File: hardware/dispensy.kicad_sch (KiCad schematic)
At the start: 20 parts, among them SW3 UP, SW4 MENU, SW5 DOWN, U1 DBT50G-7_62-4P, U18 XY300V-A-5_0-2P, U2 USB-A

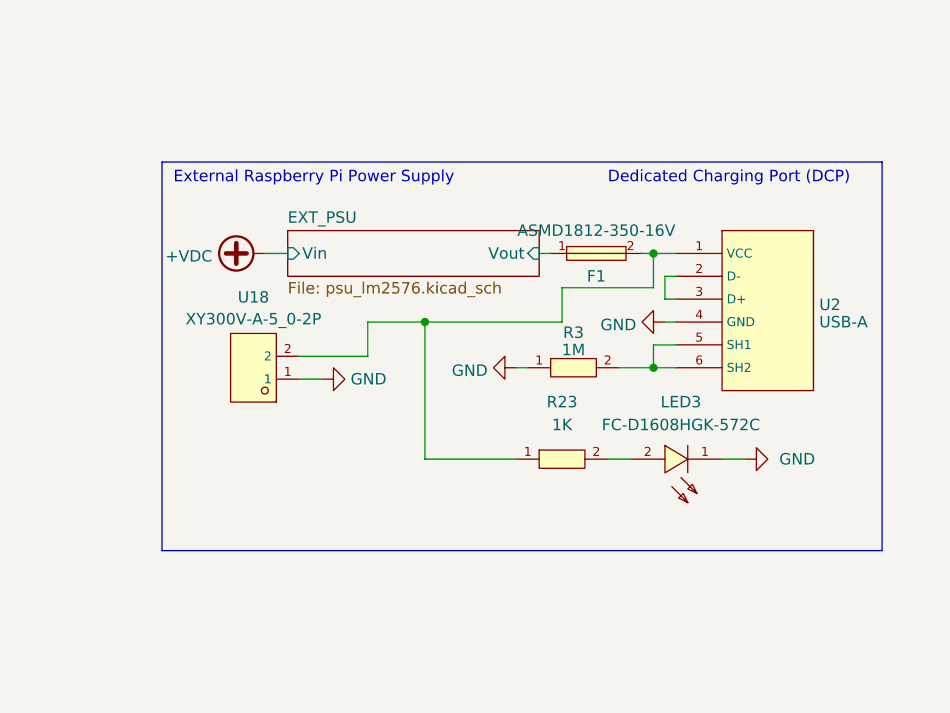
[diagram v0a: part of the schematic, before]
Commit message: replace rgb led connector with screw terminal
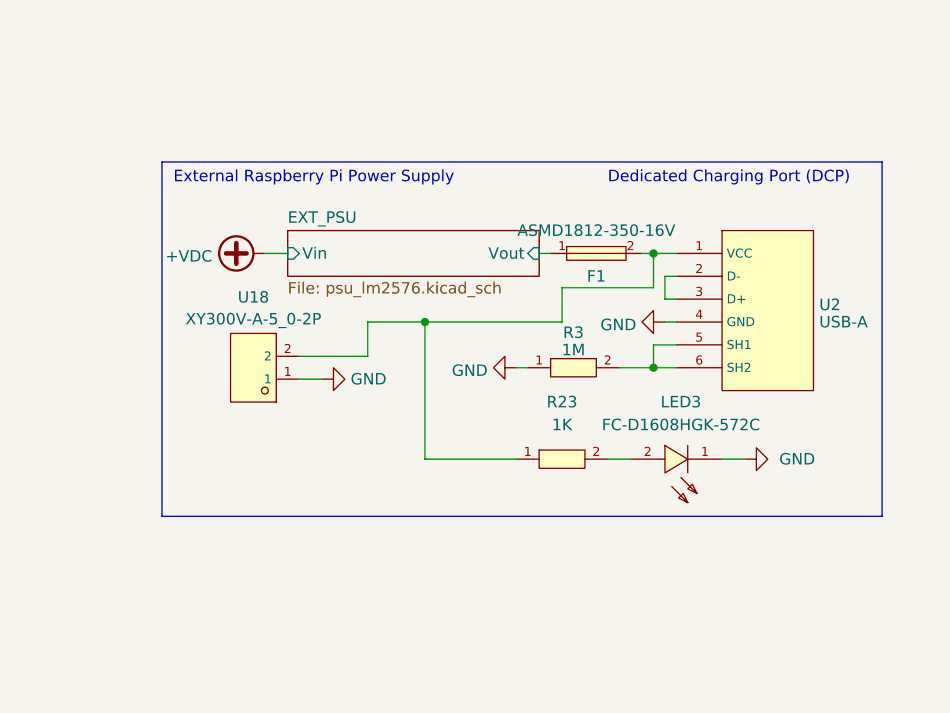
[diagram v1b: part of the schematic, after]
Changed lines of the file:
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@@
 	(title_block
 		(title "Dispensy Mainboard")
-		(date "2024-02-05")
+		(date "2024-04-06")
 		(rev "1")
 		(company "DrinkRobotics")
@@
 	(rectangle
 		(start 166.37 102.87)
-		(end 246.38 146.05)
-		(stroke
-			(width 0)
+		(end 246.38 142.24)
+		(stroke
+			(width 0)

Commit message: populate and visualize oled as 4pin header
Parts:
- OLED1: LCSC (none) -> C350310
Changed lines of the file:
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@@
+			)
+		)
+		(property "LCSC" "C350310"
+			(at 73.66 139.7 90)
+			(effects
+				(font
+					(size 1.27 1.27)
+				)
+				(hide yes)
 			)
 		)

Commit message: replace usb a with in stock part
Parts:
- U2: LCSC C386740 -> C720525
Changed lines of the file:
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@@
 			)
 		)
-		(property "LCSC" "C386740"
+		(property "LCSC" "C720525"
 			(at 231.14 120.65 0)
 			(effects
